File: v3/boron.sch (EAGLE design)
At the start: 3 parts, among them U1 BQ24168RGET, U2 ATTINY84-20MU20M1-L

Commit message: Progress on Boron eval board.
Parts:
- removed U1: BQ24168RGET, 32bits:BQ24168RGET
- removed U2: ATTINY84-20MU20M1-L, 32bits:ATTINY84-20MU20M1-L
- added C1, C3, C7, C8: 1uF, AVX_By_element14_Batch_1:06033D105KAT2A
- added C2, C6: 4.7uF, AVX_By_element14_Batch_1:08053D475KAT2A
- added C4: 47UF, AVX_By_element14_Batch_1:TAJE476K020RNJ
- added C5: 10nF, AVX_By_element14_Batch_1:06035C103KAZ2A
- added J1: batt, SparkFun-Connectors:CONN_02-JST-2MM-SMT
- added J10: USB_MINI-B_SMT, SparkFun-Connectors:USB_MINI-B_SMT
- added J11: 5.5x2.1mm Barrel, SparkFun-Connectors:POWER_JACKSMD
- added J12: out, SparkFun-Connectors:CONN_022.54MM_SCREWTERM
- added J13: debug, SparkFun-Connectors:CONN_03X2SMT
- added J4: ISP, SparkFun-Connectors:CONN_03X2SMT
- added L1: DR73-2R2-R, 32bits:DR73-2R2-R
- added L2: 1.0 uH, Bourns_By_element14_Batch_1:PM1210-1R0J-RC
- added Q1: Si7137DP, 32bits:SI7137DP
- added U2_C1: 10nF, Yageo_By_element14_Batch_1:CC0402KRX7R7BB103
- added U2_C2: 2.2uF, AVX_By_element14_Batch_1:0402ZD225KAT2A
- added U2_L1: 1 kOhm @ 100MHz, SparkFun-Resistors:RESISTOR0402
- added U2_R1, U2_R2: 10k, SparkFun-Resistors:RESISTOR0402
- added U2_R10, U2_R3, U2_R9: 100K Ohms, Vishay_By_element14_Batch_1:CRCW0402100KJNED
- added U3: ATTINY84-20MU, 32bits:ATTINY84-20MU
- added U6: TPS61230A, 32bits:TPS61230A
- added U6_CBST: 10 nF, Kemet_By_element14_Batch_1:C0402C103K5RACTU
- added U6_CFF: 10pF, Kemet_By_element14_Batch_1:C0603C100J5GACTU
- added U6_CIN: 22uF, Murata_By_element14_Batch_1:GRM21BR60J226ME39L
- added U6_COUT: 22uF, Murata_By_element14_Batch_1:GRM32ER61C226KE20L
- added U6_RFBB: 100K Ohms, Vishay_By_element14_Batch_1:CRCW0402100KFKED
- added U6_RFBT: 316K Ohms, Vishay_By_element14_Batch_1:CRCW0402316KFKED
- added U9: BQ24168RGET, 32bits:BQ24168RGET
- 5: ELEMENT (none) -> B
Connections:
- new net !RESET: J4.5, U3.PB3_(PCINT11/RESET!/DW)
- new net GND: C1.C2, C2.C2, C3.C2, C4.C1, C6.C2, C7.C2, C8.C1, J1.2, J10.GND, J11.GND, J12.2, J13.2, J4.6, U2_C1.C1, U2_C2.C2, U3.GND, U6.GND, U6_CIN.C1, U6_COUT.C1, U6_RFBB.2, U9.EPAD, U9.GND, U9.PGND, U9.PGND_2, U9.SGND
- new net MISO: J4.1, U3.PA5
- new net MOSI/SDA: J4.4, U2_L1.1, U2_L1.2, U2_R1.2, U2_R3.2, U3.PA6
- new net MOT_6V: U3.(ADC1/AIN0/PCINT1)_PA1
- new net N$1: C2.C1, U9.PMIDI
- new net N$2: J1.1, J13.5
- new net N$4: Q1.GATE, U9.BGATE
- new net N$5: C4.C2, U9.SYS, U9.SYS_2
- new net N$6: C6.C1, U9.PMIDU
- new net N$8: C7.C1, J10.VBUS, U9.USB
- new net SCK: J4.3, U2_R10.2, U2_R2.1, U3.(ADC4/USCK/SCL/T1/PCINT4)_PA4
- new net SYS_5V: J12.1, J4.2, U2_C1.C2, U2_C2.C1, U2_R10.1, U2_R3.1, U2_R9.1, U3.(ADC2/AIN1/PCINT2)_PA2, U3.VCC, U6.VOUT, U6_CFF.C2, U6_COUT.C2, U6_RFBT.1
- new net U6_CBST: U6.CBST, U6_CBST.C1
- new net U6_FB: U6.FB, U6_CFF.C1, U6_RFBB.1, U6_RFBT.2
- new net U6_SW: L2.1, U6.SW, U6_CBST.C2
- new net U9_BOOT: C5.C1, U9.BOOT
- new net U9_CD: J13.1, U9.CD
- new net U9_DRV: C8.C2, J13.3, U9.DRV, U9.TS
- new net U9_IN: C1.C1, J11.PWR, U9.IN
- new net U9_INT: U2_R9.2, U3.(ADC3/T0/PCINT3)_PA3, U9.!BATGD
- new net U9_SCL: U2_R2.2, U9.SCL
- new net U9_SDA: U2_R1.1, U9.SDA
- new net U9_STAT: U9.STAT
- new net U9_SW: C5.C2, L1.1, U9.SW
- new net VBAT: C3.C1, J13.6, Q1.DRAIN#5, Q1.DRAIN#6, Q1.DRAIN#7, Q1.DRAIN#8, U3.(ADC0/AREF/PCINT0)_PA0, U9.BAT, U9.BAT_2
- new net VCC: L1.2, L2.2, Q1.SOURCE#1, Q1.SOURCE#2, Q1.SOURCE#3, U6.EN, U6.VIN, U6_CIN.C2
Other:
- note added: "TODO: Add test points between U9 and U6"
- moved on the sheet: 5

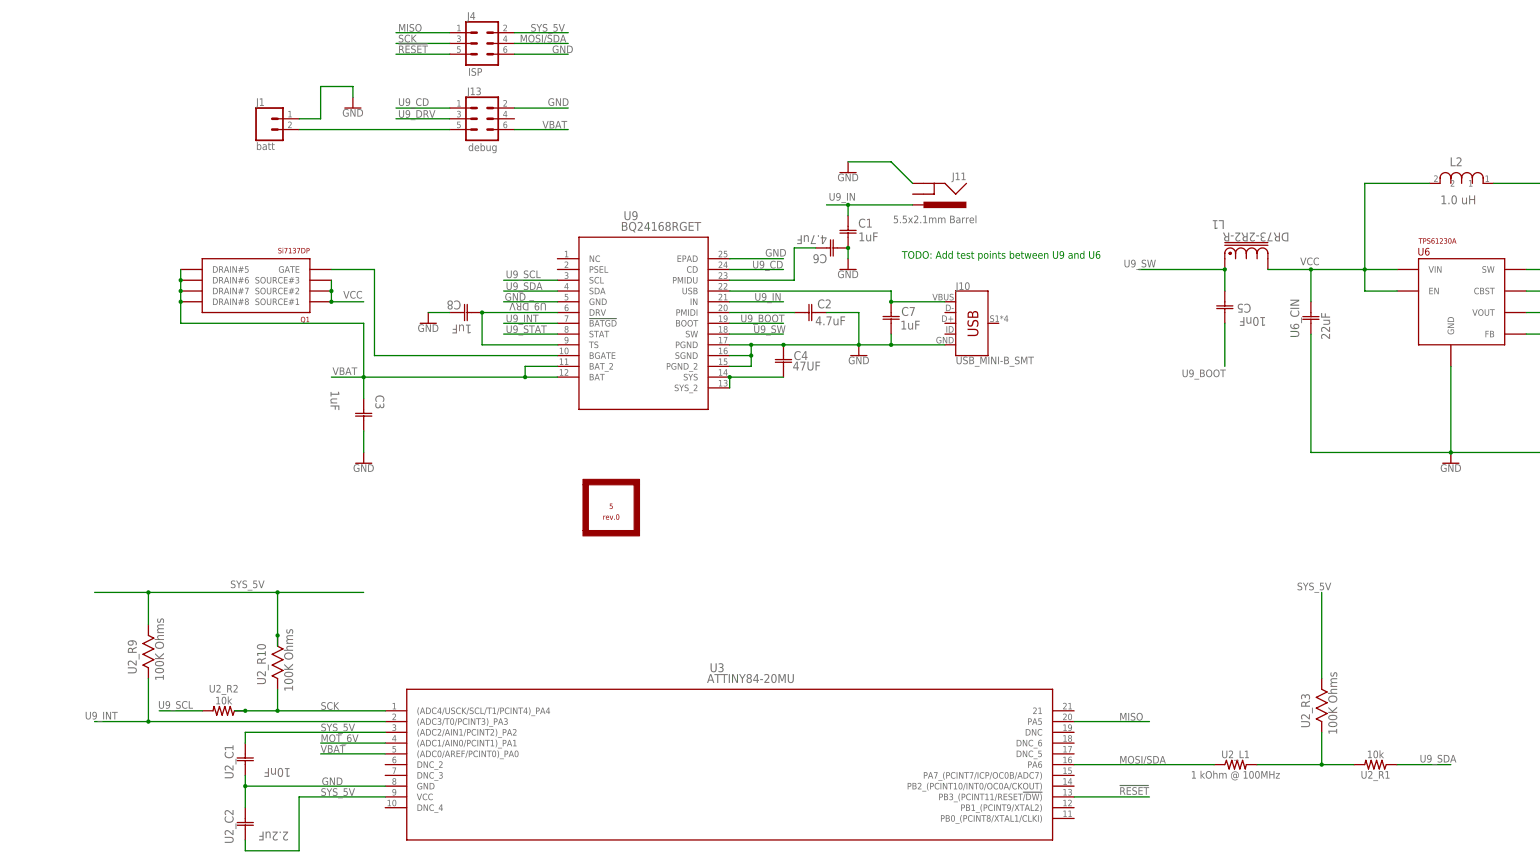
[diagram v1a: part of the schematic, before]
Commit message: Schematic Complete.
Unless I go with a different 5V supply.
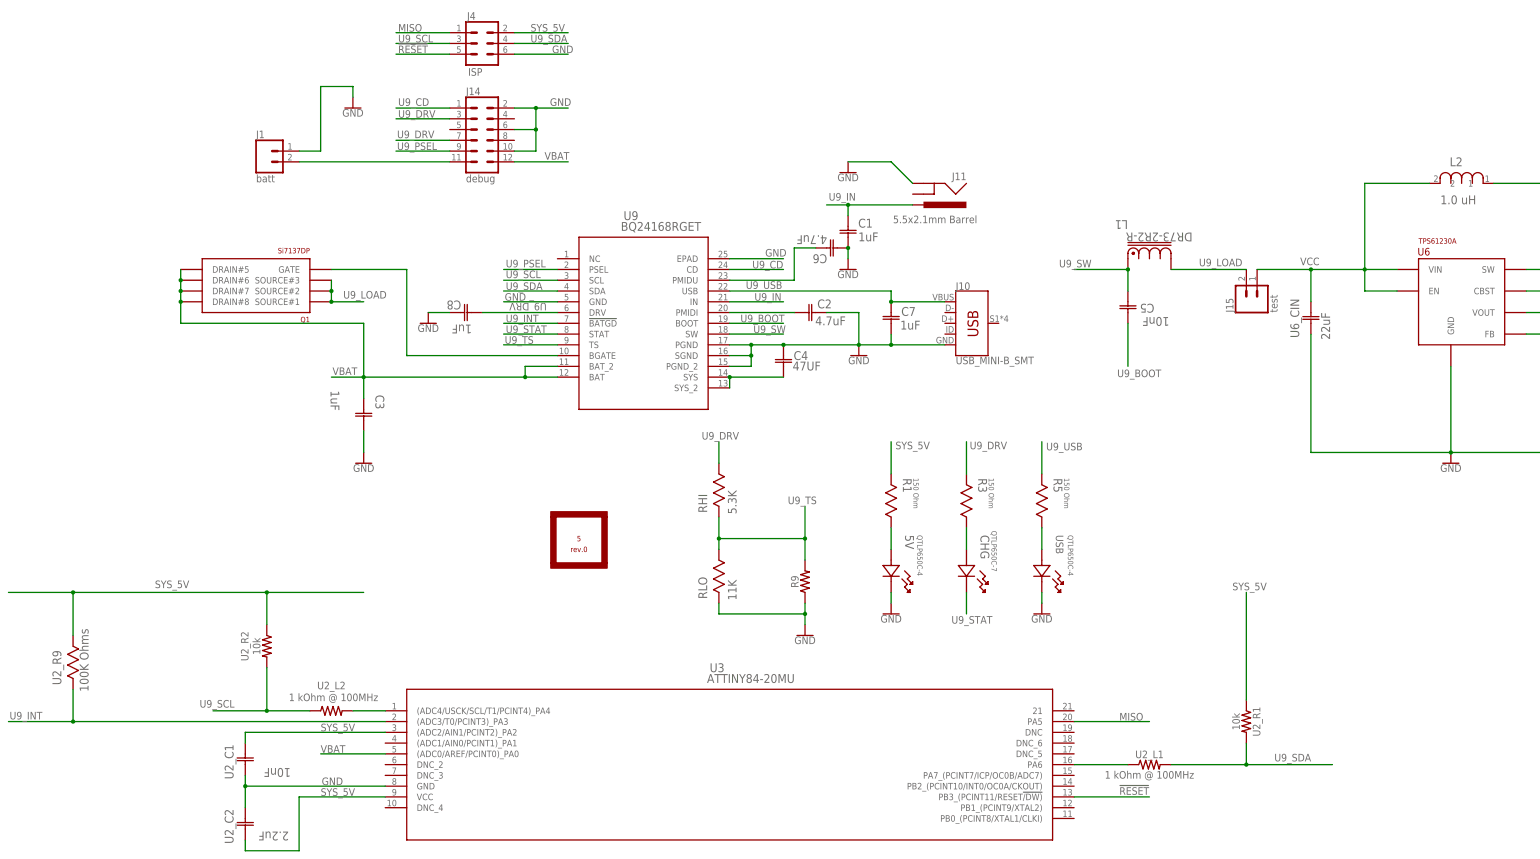
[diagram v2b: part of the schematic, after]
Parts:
- removed J13: debug, SparkFun-Connectors:CONN_03X2SMT
- removed U2_R10, U2_R3: 100K Ohms, Vishay_By_element14_Batch_1:CRCW0402100KJNED
- added 5V, USB: QTLP650C-4, Dialight_By_element14_Batch_1:597-3311-407F
- added CHG: QTLP650C-7, Dialight_By_element14_Batch_1:597-3111-407F
- added J14: debug, SparkFun-Connectors:CONN_06X2SMD_FEMALE
- added J15: test, SparkFun-Connectors:CONN_02
- added R1, R3, R5: 150 Ohm, Panasonic_By_element14_Batch_1:ERA-6AEB151V
- added R9: (no value), 32bits:NTHS1206N02N1002JE
- added RHI: 5.3K, Vishay_By_element14_Batch_1:CRCW060311K0FKEA
- added RLO: 11K, Vishay_By_element14_Batch_1:CRCW060311K0FKEA
- added U2_L2: 1 kOhm @ 100MHz, SparkFun-Resistors:RESISTOR0402
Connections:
- removed net MOT_6V: U3.(ADC1/AIN0/PCINT1)_PA1
- removed net N$8: C7.C1, J10.VBUS, U9.USB
- removed net SCK: J4.3, U2_R10.2, U2_R2.1, U3.(ADC4/USCK/SCL/T1/PCINT4)_PA4
- new net LA_5: 5V.2, R1.R1
- new net LA_CHG: CHG.2, R3.R1
- new net LA_USB: R5.R1, USB.2
- new net N$3: U2_L2.2, U3.(ADC4/USCK/SCL/T1/PCINT4)_PA4
- new net U9_LOAD: J15.2, L1.2, Q1.SOURCE#1, Q1.SOURCE#2, Q1.SOURCE#3
- new net U9_PSEL: J14.9, U9.PSEL
- new net U9_TS: R9.2, RHI.2, RLO.1, U9.TS
- new net U9_USB: C7.C1, J10.VBUS, R5.R2, U9.USB
- net GND: now also 5V.1, J14.10, J14.2, J14.6, R9.1, RLO.2, USB.1; no longer J13.2
- net MOSI/SDA: no longer J4.4, U2_L1.2, U2_R1.2, U2_R3.2
- net N$2: now also J14.11; no longer J13.5
- net SYS_5V: now also R1.R2, U2_R1.1, U2_R2.1; no longer U2_R10.1, U2_R3.1
- net U9_CD: now also J14.1; no longer J13.1
- net U9_DRV: now also J14.3, J14.7, R3.R2, RHI.1; no longer J13.3, U9.TS
- net U9_SCL: now also J4.3, U2_L2.1
- net U9_SDA: now also J4.4, U2_L1.2, U2_R1.2; no longer U2_R1.1
- net U9_STAT: now also CHG.1
- net VBAT: now also J14.12; no longer J13.6
- net VCC: now also J15.1; no longer L1.2, Q1.SOURCE#1, Q1.SOURCE#2, Q1.SOURCE#3
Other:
- note removed: "TODO: Add test points between U9 and U6"
- moved on the sheet: 5, C5, J1, L1, U2_L1, U2_R1, U2_R2, U2_R9

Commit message: Good progress on Boron layout.
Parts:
- removed J15: test, SparkFun-Connectors:CONN_02
- added J13: RASM722, 32bits:RASM722
- added J16: 5V, SparkFun-Connectors:CONN_04
- added R2, R4: 1M Ohm, Vishay_By_element14_Batch_1:CRCW06031M00JNEA
- J11: value 5.5x2.1mm Barrel -> drv; device SparkFun-Connectors:POWER_JACKSMD -> SparkFun-Connectors:CONN_04
- R9: value (none) -> 10K NTC
- RHI: value 5.3K -> 5.5K
- RLO: value 11K -> 11.6K
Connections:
- net MOSI/SDA renamed U3_PA6
- net N$1 renamed U9_PMIDI
- net N$2 renamed VBAT_CON
- net N$3 renamed U3_PA4
- net N$4 renamed U9_BGATE
- net N$6 renamed U9_PMIDU
- removed net N$5: C4.C2, U9.SYS, U9.SYS_2
- removed net U9_LOAD: J15.2, L1.2, Q1.SOURCE#1, Q1.SOURCE#2, Q1.SOURCE#3
- new net ADC0: R2.1, U3.(ADC0/AREF/PCINT0)_PA0
- new net ADC2: R4.1, U3.(ADC2/AIN1/PCINT2)_PA2
- new net U9_DRV_O: C8.C2, J11.1, U9.DRV
- new net U9_SYS: C4.C2, J16.1, L1.2, Q1.SOURCE#1, Q1.SOURCE#2, Q1.SOURCE#3, U9.SYS, U9.SYS_2
- net GND: now also J11.4, J13.GND, J16.4; no longer J11.GND
- net SYS_5V: now also R4.2; no longer U3.(ADC2/AIN1/PCINT2)_PA2
- net U9_DRV: now also J11.2, J11.3; no longer C8.C2, U9.DRV
- net U9_IN: now also J13.PWR; no longer J11.PWR
- net VBAT: now also R2.2; no longer U3.(ADC0/AREF/PCINT0)_PA0
- net VCC: now also J16.2, J16.3; no longer J15.1
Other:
- moved on the sheet: C8, U2_C1, U2_C2

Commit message: Boron off to OSH.
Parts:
- removed C4: 47UF, AVX_By_element14_Batch_1:TAJE476K020RNJ
- removed C6: 4.7uF, AVX_By_element14_Batch_1:08053D475KAT2A
- removed U2_C1: 10nF, Yageo_By_element14_Batch_1:CC0402KRX7R7BB103
- added U9_C4: 47uF, AVX_By_element14_Batch_1:12067C332KAT2A
- added U9_C6: 4.7uF, AVX_By_element14_Batch_1:08053D475KAT2A
- J14: device SparkFun-Connectors:CONN_06X2SMD_FEMALE -> SparkFun-Connectors:CONN_06X2PTH_FEMALE
- J4: device SparkFun-Connectors:CONN_03X2SMT -> SparkFun-Connectors:CONN_03X2FEMALE
- renumbered C2 to U9_C2, C5 to U9_C5, L1 to U9_L1
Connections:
- removed net U9_DRV_O: C8.C2, J11.1, U9.DRV
- new net U9_DRV_0: J11.2, J11.3, U9.DRV
- net GND: now also U3.21, U9_C4.C1, U9_C6.C2; no longer C4.C1, C6.C2, U2_C1.C1
- net SYS_5V: no longer U2_C1.C2
- net U9_DRV: now also C8.C2, J11.1; no longer J11.2, J11.3
- net U9_PMIDU: now also U9_C6.C1; no longer C6.C1
- net U9_SYS: now also U9_C4.C2; no longer C4.C2
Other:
- moved on the sheet: C1

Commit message: Boron R0 send to OSH part + NOTIFY.
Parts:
- added NOTIFY: QTLP650C-4, Dialight_By_element14_Batch_1:597-3311-407F
- added R6: 150 Ohm, Panasonic_By_element14_Batch_1:ERA-6AEB151V
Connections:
- new net 1ROU: R6.R2, U3.PA7_(PCINT7/ICP/OC0B/ADC7)
- new net LA_1: NOTIFY.2, R6.R1
- net GND: now also NOTIFY.1
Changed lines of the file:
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@@
 <part name="J11" library="SparkFun-Connectors" deviceset="CONN_04" device="" value="drv"/>
 <part name="J16" library="SparkFun-Connectors" deviceset="CONN_04" device="" value="5V"/>
+<part name="NOTIFY" library="Dialight_By_element14_Batch_1" deviceset="597-3311-407F" device="" value="QTLP650C-4"/>
+<part name="GND11" library="SparkFun-PowerSymbols" deviceset="GND" device=""/>
+<part name="R6" library="Panasonic_By_element14_Batch_1" deviceset="ERA-6AEB151V" device="" value="150 Ohm"/>
 </parts>
 <sheets>
@@
 </instance>
 <instance part="GND8" gate="1" x="294.64" y="73.66"/>
-<instance part="U2_L1" gate="G$1" x="127" y="-60.96"/>
+<instance part="U2_L1" gate="G$1" x="127" y="-60.96" smashed="yes">
+<attribute name="NAME" x="127" y="-59.436" size="1.778" layer="95" font="vector" align="bottom-center"/>
+<attribute name="VALUE" x="135.128" y="-62.23" size="1.778" layer="96" font="vector" align="top-center"/>
+</instance>
 <instance part="U2_L2" gate="G$1" x="-66.04" y="-48.26" smashed="yes">
 <attribute name="NAME" x="-66.04" y="-43.18" size="1.778" layer="95" font="vector" align="bottom-center"/>
@@
 <instance part="J11" gate="G$1" x="-27.94" y="129.54"/>
 <instance part="J16" gate="G$1" x="-27.94" y="152.4"/>
+<instance part="NOTIFY" gate="A" x="119.38" y="-10.16" smashed="yes" rot="R270">
+<attribute name="VALUE" x="125.5268" y="-6.7818" size="1.27" layer="96" ratio="10" rot="SR270"/>
+<attribute name="NAME" x="122.428" y="-3.4544" size="2.0828" layer="95" ratio="10" rot="SR270"/>
+</instance>
+<instance part="GND11" gate="1" x="119.38" y="-25.4"/>
+<instance part="R6" gate="A" x="119.38" y="7.62" smashed="yes" rot="R270">
+<attribute name="VALUE" x="124.6124" y="6.6802" size="1.27" layer="96" ratio="10" rot="SR270"/>
+<attribute name="NAME" x="122.1486" y="6.6294" size="2.0828" layer="95" ratio="10" rot="SR270"/>
+</instance>
 </instances>
 <busses>
@@
 <label x="120.904" y="-48.006" size="1.778" layer="95"/>
 </segment>
+<segment>
+<pinref part="NOTIFY" gate="A" pin="1"/>
+<wire x1="119.38" y1="-20.32" x2="119.38" y2="-22.86" width="0.1524" layer="91"/>
+<pinref part="GND11" gate="1" pin="GND"/>
+</segment>
 </net>
 <net name="VBAT" class="0">
@@
 </segment>
 </net>
+<net name="LA_1" class="0">
+<segment>
+<pinref part="NOTIFY" gate="A" pin="2"/>
+<wire x1="119.38" y1="-10.16" x2="119.38" y2="-5.08" width="0.1524" layer="91"/>
+<pinref part="R6" gate="A" pin="R1"/>
+</segment>
+</net>
+<net name="1ROU" class="0">
+<segment>
+<pinref part="U3" gate="A" pin="PA7_(PCINT7/ICP/OC0B/ADC7)"/>
+<wire x1="109.22" y1="-63.5" x2="121.92" y2="-63.5" width="0.1524" layer="91"/>
+<label x="113.03" y="-63.246" size="1.778" layer="95"/>
+</segment>
+<segment>
+<wire x1="119.38" y1="7.62" x2="119.38" y2="15.24" width="0.1524" layer="91"/>
+<label x="120.396" y="13.462" size="1.778" layer="95"/>
+<pinref part="R6" gate="A" pin="R2"/>
+</segment>
+</net>

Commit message: Boron r.1 off to OSH park.
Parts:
- 5: value rev.0 -> rev.1
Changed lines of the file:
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@@
 <part name="J10" library="SparkFun-Connectors" deviceset="USB_MINI-B" device="_SMT"/>
 <part name="J4" library="SparkFun-Connectors" deviceset="CONN_03X2" device="FEMALE" value="ISP"/>
-<part name="5" library="32bits" deviceset="PERIODIC_SYMBOL" device="" value="rev.0">
+<part name="5" library="32bits" deviceset="PERIODIC_SYMBOL" device="" value="rev.1">
 <attribute name="ELEMENT" value="B"/>
 </part>
@@
 <net name="VBAT" class="0">
 <segment>
+<pinref part="J14" gate="G$1" pin="12"/>
+<wire x1="-22.86" y1="81.28" x2="-10.16" y2="81.28" width="0.1524" layer="91"/>
+<label x="-15.748" y="81.788" size="1.778" layer="95"/>
+</segment>
+<segment>
+<pinref part="R2" gate="A" pin="2"/>
+<wire x1="-68.58" y1="-58.42" x2="-76.2" y2="-58.42" width="0.1524" layer="91"/>
+<label x="-75.946" y="-58.166" size="1.778" layer="95"/>
+</segment>
+<segment>
 <pinref part="U9" gate="A" pin="BAT"/>
 <pinref part="U9" gate="A" pin="BAT_2"/>
@@
 <wire x1="-58.42" y1="25.4" x2="-58.42" y2="30.48" width="0.1524" layer="91"/>
 <junction x="-58.42" y="30.48"/>
-<pinref part="Q1" gate="G$1" pin="DRAIN#8"/>
-<wire x1="-101.6" y1="48.26" x2="-101.6" y2="43.18" width="0.1524" layer="91"/>
-<wire x1="-101.6" y1="43.18" x2="-58.42" y2="43.18" width="0.1524" layer="91"/>
-<wire x1="-58.42" y1="43.18" x2="-58.42" y2="30.48" width="0.1524" layer="91"/>
-<pinref part="Q1" gate="G$1" pin="DRAIN#7"/>
-<wire x1="-101.6" y1="48.26" x2="-101.6" y2="50.8" width="0.1524" layer="91"/>
-<junction x="-101.6" y="48.26"/>
-<pinref part="Q1" gate="G$1" pin="DRAIN#6"/>
-<wire x1="-101.6" y1="50.8" x2="-101.6" y2="53.34" width="0.1524" layer="91"/>
-<junction x="-101.6" y="50.8"/>
-<pinref part="Q1" gate="G$1" pin="DRAIN#5"/>
-<wire x1="-101.6" y1="53.34" x2="-101.6" y2="55.88" width="0.1524" layer="91"/>
-<junction x="-101.6" y="53.34"/>
 <label x="-65.786" y="30.988" size="1.778" layer="95"/>
 <wire x1="-58.42" y1="30.48" x2="-66.04" y2="30.48" width="0.1524" layer="91"/>
 </segment>
 <segment>
-<pinref part="J14" gate="G$1" pin="12"/>
-<wire x1="-22.86" y1="81.28" x2="-10.16" y2="81.28" width="0.1524" layer="91"/>
-<label x="-15.748" y="81.788" size="1.778" layer="95"/>
-</segment>
-<segment>
-<pinref part="R2" gate="A" pin="2"/>
-<wire x1="-68.58" y1="-58.42" x2="-76.2" y2="-58.42" width="0.1524" layer="91"/>
-<label x="-75.946" y="-58.166" size="1.778" layer="95"/>
+<pinref part="Q1" gate="G$1" pin="DRAIN#5"/>
+<wire x1="-101.6" y1="55.88" x2="-116.84" y2="55.88" width="0.1524" layer="91"/>
+<label x="-116.84" y="56.388" size="1.778" layer="95"/>
+<pinref part="Q1" gate="G$1" pin="DRAIN#6"/>
+<wire x1="-101.6" y1="55.88" x2="-101.6" y2="53.34" width="0.1524" layer="91"/>
+<junction x="-101.6" y="55.88"/>
+<pinref part="Q1" gate="G$1" pin="DRAIN#7"/>
+<wire x1="-101.6" y1="53.34" x2="-101.6" y2="50.8" width="0.1524" layer="91"/>
+<junction x="-101.6" y="53.34"/>
+<pinref part="Q1" gate="G$1" pin="DRAIN#8"/>
+<wire x1="-101.6" y1="50.8" x2="-101.6" y2="48.26" width="0.1524" layer="91"/>
+<junction x="-101.6" y="50.8"/>
 </segment>
 </net>
@@
 </segment>
 <segment>
-<pinref part="Q1" gate="G$1" pin="SOURCE#3"/>
-<pinref part="Q1" gate="G$1" pin="SOURCE#2"/>
-<wire x1="-66.04" y1="53.34" x2="-66.04" y2="50.8" width="0.1524" layer="91"/>
-<pinref part="Q1" gate="G$1" pin="SOURCE#1"/>
-<wire x1="-66.04" y1="50.8" x2="-66.04" y2="48.26" width="0.1524" layer="91"/>
-<junction x="-66.04" y="50.8"/>
-<wire x1="-66.04" y1="48.26" x2="-58.42" y2="48.26" width="0.1524" layer="91"/>
-<junction x="-66.04" y="48.26"/>
-<label x="-63.246" y="49.022" size="1.778" layer="95"/>
-</segment>
-<segment>
 <pinref part="J16" gate="G$1" pin="1"/>
 <wire x1="-22.86" y1="149.86" x2="-10.16" y2="149.86" width="0.1524" layer="91"/>
 <label x="-14.986" y="150.114" size="1.778" layer="95"/>
 </segment>
-</net>
+<segment>
+<pinref part="Q1" gate="G$1" pin="SOURCE#1"/>
+<pinref part="Q1" gate="G$1" pin="SOURCE#2"/>
+<pinref part="Q1" gate="G$1" pin="SOURCE#3"/>
+<wire x1="-66.04" y1="53.34" x2="-66.04" y2="50.8" width="0.1524" layer="91"/>
+<junction x="-66.04" y="50.8"/>
+<wire x1="-66.04" y1="50.8" x2="-66.04" y2="48.26" width="0.1524" layer="91"/>
+<junction x="-66.04" y="48.26"/>
+<wire x1="-66.04" y1="48.26" x2="-58.42" y2="48.26" width="0.1524" layer="91"/>
+<label x="-63.246" y="49.022" size="1.778" layer="95"/>
+</segment>
+</net>

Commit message: Fixing the stupid backwards USB port.
Doh!
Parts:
- 5: value rev.1 -> rev.2
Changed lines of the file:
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@@
 <part name="J10" library="SparkFun-Connectors" deviceset="USB_MINI-B" device="_SMT"/>
 <part name="J4" library="SparkFun-Connectors" deviceset="CONN_03X2" device="FEMALE" value="ISP"/>
-<part name="5" library="32bits" deviceset="PERIODIC_SYMBOL" device="" value="rev.1">
+<part name="5" library="32bits" deviceset="PERIODIC_SYMBOL" device="" value="rev.2">
 <attribute name="ELEMENT" value="B"/>
 </part>

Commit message: Boron R.3 off to osh park.
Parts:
- 5: value rev.2 -> rev.3
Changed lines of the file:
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@@
 <part name="J10" library="SparkFun-Connectors" deviceset="USB_MINI-B" device="_SMT"/>
 <part name="J4" library="SparkFun-Connectors" deviceset="CONN_03X2" device="FEMALE" value="ISP"/>
-<part name="5" library="32bits" deviceset="PERIODIC_SYMBOL" device="" value="rev.2">
+<part name="5" library="32bits" deviceset="PERIODIC_SYMBOL" device="" value="rev.3">
 <attribute name="ELEMENT" value="B"/>
 </part>
